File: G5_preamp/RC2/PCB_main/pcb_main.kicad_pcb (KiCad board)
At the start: 2 copper layers, 165 x 58 mm, 57 parts, among them J1 PSU_TUBE, J2 PCB_TUBE, J3 PSU_AMP, J4 AMP, J5 PSU_SIMCAB, J6 SIMCAB, J7 3PDT, J8 LEVEL 3-2, Q1 MPS751, Q2 IRF740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

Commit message: DC jack Polarity change
DC Jack polarity change and some capacitor footprint mod
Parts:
- added REF**: PG5_Logo_15mm_SilkScreen, Symbol:PG5_Logo_15mm_SilkScreen, F.Cu at (169.2, 118.7)
- C17: value 4.7µ/350V -> 4.7µ/400V
- C6: footprint Capacitor_THT:CP_Radial_D6.3mm_P2.50mm -> Capacitor_THT:CP_Radial_D5.0mm_P2.00mm
- moved C6 0.46 mm to (112.5, 145.9)
- renumbered R3 to R6, XLR_1 to XLR1, XLR_2 to XLR2, XLR_3 to XLR3
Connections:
- DC1 pad 1: GNDREF -> +24V
- DC1 pad 2: +24V -> GNDREF
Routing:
- net +24V: track 194.0 -> 197.0 mm

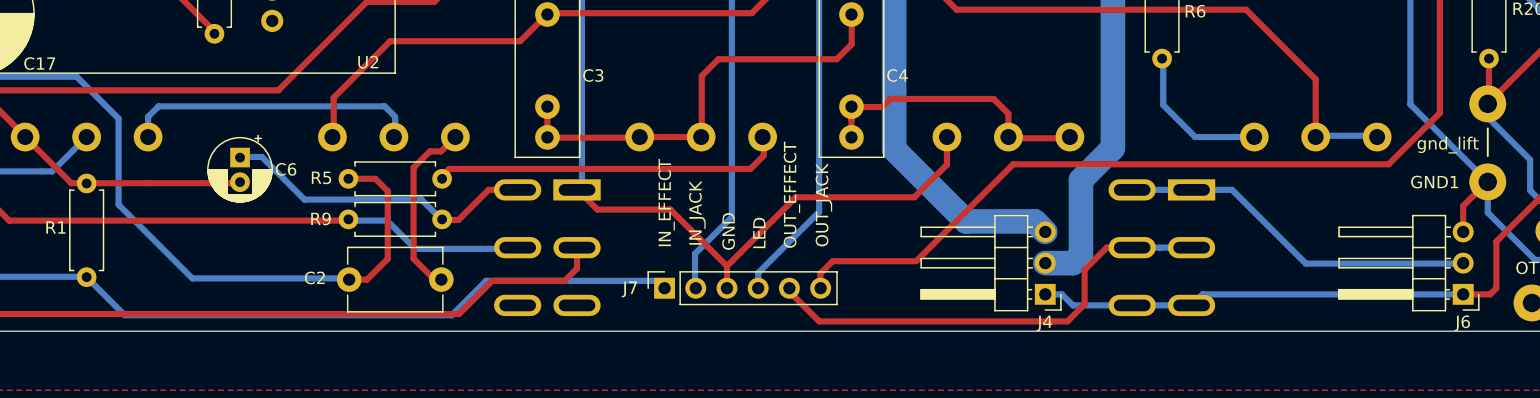
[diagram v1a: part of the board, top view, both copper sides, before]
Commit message: Reverse SimulHP switch
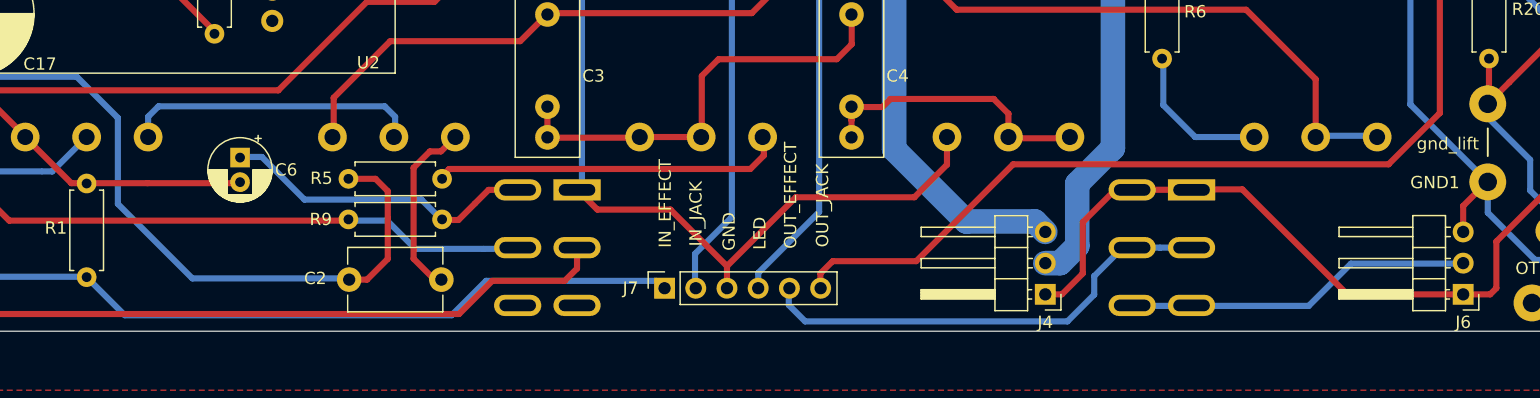
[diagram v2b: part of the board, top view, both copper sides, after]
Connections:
- SW2 pad 1: /SIMCAB_OUT -> /LINE_OUT
- SW2 pad 3: /LINE_OUT -> /SIMCAB_OUT
- SW2 pad 4: /SIMCAB_OUT -> /LINE_OUT
- SW2 pad 6: /LINE_OUT -> /SIMCAB_OUT
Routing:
- net /LINE_OUT: track 57.3 -> 65.5 mm
- net /SIMCAB_OUT: track 29.3 -> 28.3 mm
- net /HP1: track 39.9 -> 39.3 mm
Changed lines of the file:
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@@
     (thickness 1.6)
     (drawings 23)
-    (tracks 351)
+    (tracks 355)
     (zones 0)
     (modules 58)
@@
     (fp_line (start -3.28 1.77) (end 8.36 1.77) (layer B.SilkS) (width 0.12))
     (pad 1 thru_hole rect (at 0 0 180) (size 3.85 1.73) (drill oval 2.99 0.96) (layers *.Cu *.Mask)
-      (net 5 /SIMCAB_OUT))
+      (net 23 /LINE_OUT))
     (pad 2 thru_hole oval (at 0 -4.7 180) (size 3.85 1.73) (drill oval 2.99 0.96) (layers *.Cu *.Mask)
       (net 32 /OUT_EFFECT))
     (pad 3 thru_hole oval (at 0 -9.4 180) (size 3.85 1.73) (drill oval 2.99 0.96) (layers *.Cu *.Mask)
-      (net 23 /LINE_OUT))
+      (net 5 /SIMCAB_OUT))
     (pad 5 thru_hole oval (at 4.83 -4.7 180) (size 3.85 1.73) (drill oval 2.99 0.96) (layers *.Cu *.Mask)
       (net 32 /OUT_EFFECT))
     (pad 6 thru_hole oval (at 4.83 -9.4 180) (size 3.85 1.73) (drill oval 2.99 0.96) (layers *.Cu *.Mask)
-      (net 23 /LINE_OUT))
-    (pad 4 thru_hole oval (at 4.83 0 180) (size 3.85 1.73) (drill oval 2.99 0.96) (layers *.Cu *.Mask)
       (net 5 /SIMCAB_OUT))
+    (pad 4 thru_hole oval (at 4.83 0 180) (size 3.85 1.73) (drill oval 2.99 0.96) (layers *.Cu *.Mask)
+      (net 23 /LINE_OUT))
     (model ${KISYS3DMOD}/Button_Switch_THT.3dshapes/SW_CK_Lever_DPDT_72xx.wrl
       (at (xyz 0 0 0))
@@
   (segment (start 135.28 136.4) (end 137.56 134.12) (width 0.5) (layer F.Cu) (net 4))
   (segment (start 137.56 134.12) (end 154.12 134.12) (width 0.5) (layer F.Cu) (net 4))
-  (segment (start 199.2 154.5) (end 212 154.5) (width 0.5) (layer B.Cu) (net 5) (status 20))
-  (segment (start 185.17 148.5) (end 193.2 148.5) (width 0.5) (layer B.Cu) (net 5) (status 10))
-  (segment (start 193.2 148.5) (end 199.2 154.5) (width 0.5) (layer B.Cu) (net 5))
+  (segment (start 202.87 154.5) (end 212 154.5) (width 0.5) (layer B.Cu) (net 5))
+  (segment (start 199.43 157.94) (end 202.87 154.5) (width 0.5) (layer B.Cu) (net 5))
+  (segment (start 185.09 157.91) (end 185.12 157.94) (width 0.5) (layer B.Cu) (net 5))
+  (segment (start 185.12 157.94) (end 199.43 157.94) (width 0.5) (layer B.Cu) (net 5))
   (segment (start 104.9 144.2) (end 105 144.1) (width 0.5) (layer F.Cu) (net 6) (status 30))
   (segment (start 125.1 142.55) (end 125.1 143.2) (width 0.5) (layer B.Cu) (net 6) (status 20))
@@
   (segment (start 123.5 147.6) (end 121.3 147.6) (width 0.5) (layer F.Cu) (net 9) (status 20))
   (segment (start 108.6 155.7) (end 121.4 155.7) (width 0.5) (layer B.Cu) (net 9))
-  (segment (start 102.6 149.7) (end 108.6 155.7) (width 0.5) (layer B.Cu) (net 9))
-  (segment (start 102.6 142.7) (end 102.6 149.7) (width 0.5) (layer B.Cu) (net 9))
+  (segment (start 102.54 149.64) (end 108.6 155.7) (width 0.5) (layer B.Cu) (net 9))
+  (segment (start 102.54 142.64) (end 102.54 149.64) (width 0.5) (layer B.Cu) (net 9))
   (segment (start 82 139.3) (end 99.2 139.3) (width 0.5) (layer B.Cu) (net 9))
-  (segment (start 99.2 139.3) (end 102.6 142.7) (width 0.5) (layer B.Cu) (net 9))
+  (segment (start 99.2 139.3) (end 102.54 142.64) (width 0.5) (layer B.Cu) (net 9))
   (segment (start 82.1 147) (end 82 146.9) (width 0.5) (layer F.Cu) (net 10) (status 30))
   (segment (start 96.3 147) (end 82.1 147) (width 0.5) (layer B.Cu) (net 10) (status 20))
@@
   (segment (start 130.3 158.6) (end 133 155.9) (width 0.5) (layer F.Cu) (net 22))
   (segment (start 226.8 144.2) (end 225 144.2) (width 0.5) (layer F.Cu) (net 23) (status 30))
+  (segment (start 183.69 148.49) (end 189.96 148.49) (width 0.5) (layer F.Cu) (net 23))
+  (segment (start 181.05 151.13) (end 183.69 148.49) (width 0.5) (layer F.Cu) (net 23))
+  (segment (start 181.05 155.3) (end 181.05 151.13) (width 0.5) (layer F.Cu) (net 23))
+  (segment (start 178 157) (end 179.35 157) (width 0.5) (layer F.Cu) (net 23))
+  (segment (start 179.35 157) (end 181.05 155.3) (width 0.5) (layer F.Cu) (net 23))
+  (segment (start 214.7 156.5) (end 214.2 157) (width 0.5) (layer F.Cu) (net 23))
+  (segment (start 214.7 152.7) (end 214.7 156.5) (width 0.5) (layer F.Cu) (net 23))
+  (segment (start 218.7 148.7) (end 214.7 152.7) (width 0.5) (layer F.Cu) (net 23))
+  (segment (start 220.5 148.7) (end 218.7 148.7) (width 0.5) (layer F.Cu) (net 23))
   (segment (start 225 144.2) (end 223.079999 146.120001) (width 0.5) (layer F.Cu) (net 23) (status 10))
   (segment (start 223.079999 146.120001) (end 220.5 148.7) (width 0.5) (layer F.Cu) (net 23))
-  (segment (start 220.5 148.7) (end 218.7 148.7) (width 0.5) (layer F.Cu) (net 23))
-  (segment (start 218.7 148.7) (end 214.7 152.7) (width 0.5) (layer F.Cu) (net 23))
-  (segment (start 214.7 152.7) (end 214.7 156.5) (width 0.5) (layer F.Cu) (net 23))
-  (segment (start 214.7 156.5) (end 214.2 157) (width 0.5) (layer F.Cu) (net 23))
   (segment (start 214.2 157) (end 212 157) (width 0.5) (layer F.Cu) (net 23) (status 20))
-  (segment (start 179.35 157) (end 180.25 157.9) (width 0.5) (layer B.Cu) (net 23))
-  (segment (start 178 157) (end 179.35 157) (width 0.5) (layer B.Cu) (net 23) (status 10))
-  (segment (start 180.25 157.9) (end 185.1 157.9) (width 0.5) (layer B.Cu) (net 23) (status 20))
-  (segment (start 185.1 157.9) (end 190.1 157.9) (width 0.5) (layer B.Cu) (net 23) (status 30))
-  (segment (start 212 157) (end 190.8 157) (width 0.5) (layer B.Cu) (net 23) (status 10))
-  (segment (start 190.8 157) (end 189.9 157.9) (width 0.5) (layer B.Cu) (net 23) (status 20))
+  (segment (start 194.03 148.46) (end 190.3 148.46) (width 0.5) (layer F.Cu) (net 23))
+  (segment (start 212 157) (end 202.57 157) (width 0.5) (layer F.Cu) (net 23))
+  (segment (start 202.57 157) (end 194.03 148.46) (width 0.5) (layer F.Cu) (net 23))
   (segment (start 179.6 103.5) (end 181.9 105.8) (width 2) (layer B.Cu) (net 24) (status 20))
   (segment (start 177.150001 151.070001) (end 171.570001 151.070001) (width 2) (layer B.Cu) (net 24) (status 10))
@@
   (segment (start 165.7 110.3) (end 172.5 103.5) (width 2) (layer B.Cu) (net 24))
   (segment (start 172.5 103.5) (end 179.6 103.5) (width 2) (layer B.Cu) (net 24))
-  (segment (start 183.5 120.3) (end 182 118.8) (width 2) (layer B.Cu) (net 25) (status 20))
+  (segment (start 183.5 120.3) (end 182 118.8) (width 2) (layer B.Cu) (net 25))
   (segment (start 183.5 145.1) (end 183.5 120.3) (width 2) (layer B.Cu) (net 25))
-  (segment (start 180.9 147.7) (end 183.5 145.1) (width 2) (layer B.Cu) (net 25))
-  (segment (start 180.9 153.8) (end 180.9 147.7) (width 2) (layer B.Cu) (net 25))
-  (segment (start 178 154.46) (end 180.24 154.46) (width 2) (layer B.Cu) (net 25) (status 10))
-  (segment (start 180.24 154.46) (end 180.9 153.8) (width 2) (layer B.Cu) (net 25))
+  (segment (start 180.599989 148.000011) (end 183.5 145.1) (width 2) (layer B.Cu) (net 25))
+  (segment (start 180.599989 153.062092) (end 180.599989 148.000011) (width 2) (layer B.Cu) (net 25))
+  (segment (start 179.202081 154.46) (end 180.599989 153.062092) (width 2) (layer B.Cu) (net 25))
+  (segment (start 178 154.46) (end 179.202081 154.46) (width 2) (layer B.Cu) (net 25))
   (segment (start 138.5 118.8) (end 138.5 118.7) (width 0.5) (layer B.Cu) (net 30))
   (segment (start 152.5 132.8) (end 138.5 118.8) (width 0.5) (layer B.Cu) (net 30))
@@
   (segment (start 185.17 153.2) (end 187.345 153.2) (width 0.5) (layer B.Cu) (net 32) (status 10))
   (segment (start 187.345 153.2) (end 190.1 153.2) (width 0.5) (layer B.Cu) (net 32) (status 20))
-  (segment (start 159.59999 159.19999) (end 156.9 156.5) (width 0.5) (layer F.Cu) (net 32))
-  (segment (start 179.80001 159.19999) (end 159.59999 159.19999) (width 0.5) (layer F.Cu) (net 32))
-  (segment (start 181.2 157.8) (end 179.80001 159.19999) (width 0.5) (layer F.Cu) (net 32))
-  (segment (start 181.2 154.995) (end 181.2 157.8) (width 0.5) (layer F.Cu) (net 32))
-  (segment (start 185.17 153.2) (end 182.995 153.2) (width 0.5) (layer F.Cu) (net 32) (status 10))
-  (segment (start 182.995 153.2) (end 181.2 154.995) (width 0.5) (layer F.Cu) (net 32))
+  (segment (start 185.17 153.2) (end 184.29 153.2) (width 0.5) (layer F.Cu) (net 32))
+  (segment (start 157.13 157.87) (end 157.13 156.56) (width 0.5) (layer B.Cu) (net 32))
+  (segment (start 158.45999 159.19999) (end 157.13 157.87) (width 0.5) (layer B.Cu) (net 32))
+  (segment (start 179.80001 159.19999) (end 158.45999 159.19999) (width 0.5) (layer B.Cu) (net 32))
+  (segment (start 181.98 157.02) (end 179.80001 159.19999) (width 0.5) (layer B.Cu) (net 32))
+  (segment (start 184.29 153.2) (end 181.98 155.51) (width 0.5) (layer B.Cu) (net 32))
+  (segment (start 181.98 155.51) (end 181.98 157.02) (width 0.5) (layer B.Cu) (net 32))
   (segment (start 159.7 155.3) (end 159.7 156.5) (width 0.5) (layer F.Cu) (net 33))
   (segment (start 160.7 154.3) (end 159.7 155.3) (width 0.5) (layer F.Cu) (net 33))
